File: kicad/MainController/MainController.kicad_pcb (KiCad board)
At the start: 2 copper layers, 45 parts, among them J1 Controller, J10 Barrel_Jack_Switch, J3 JTAG, J4 H-Bridge, J5 Lamp, J7 RGB, J8 Winch, J9 Motor, Q1 BC547, Q10 BUZ11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

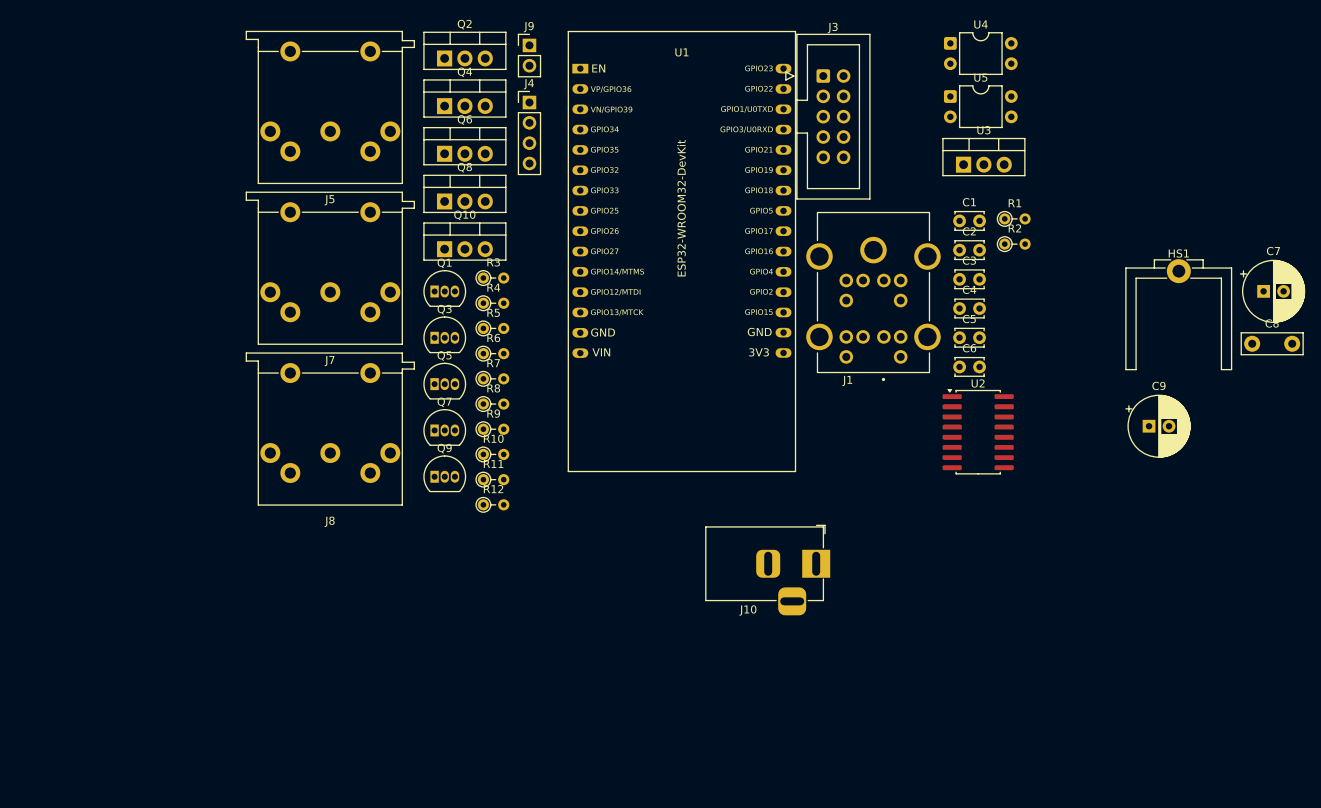
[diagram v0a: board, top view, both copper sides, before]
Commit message: New main controller PCB layout using ESP32
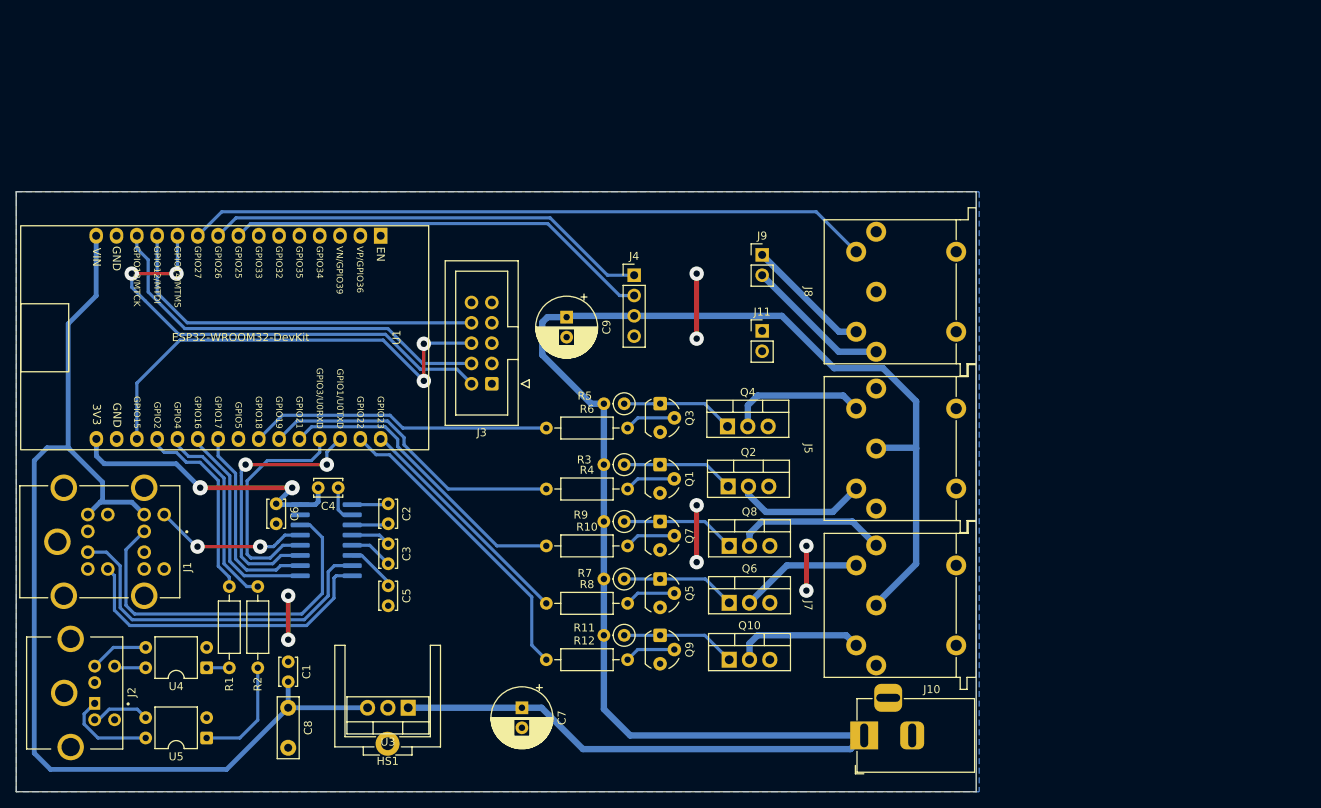
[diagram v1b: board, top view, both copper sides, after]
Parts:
- added J11: Pwr, Connector_PinHeader_2.54mm:PinHeader_1x02_P2.54mm_Vertical, F.Cu at (170.7, 85.4)
- added J2: Screen, SnapEDA:MiniDIN TE_5749180-1, F.Cu at (83.5, 130.7)
- Q1, Q3, Q5, Q7, Q9: footprint Package_TO_SOT_THT:TO-92_Inline -> Custom_Footprints:TO-92_Milling
- R1, R2: footprint Resistor_THT:R_Axial_DIN0204_L3.6mm_D1.6mm_P2.54mm_Vertical -> Resistor_THT:R_Axial_DIN0207_L6.3mm_D2.5mm_P10.16mm_Horizontal
- R10, R12, R4, R6, R8: value 220 -> 1k; footprint Resistor_THT:R_Axial_DIN0204_L3.6mm_D1.6mm_P2.54mm_Vertical -> Resistor_THT:R_Axial_DIN0207_L6.3mm_D2.5mm_P10.16mm_Horizontal
- R11, R3, R5, R7, R9: footprint Resistor_THT:R_Axial_DIN0204_L3.6mm_D1.6mm_P2.54mm_Vertical -> Resistor_THT:R_Axial_DIN0207_L6.3mm_D2.5mm_P2.54mm_Vertical
- U2: moved to B.Cu
- moved C8 128.8 mm to (111.5, 132.5), turned to -90 degrees
- moved U5 122.8 mm to (101.3, 136.3), turned to 180 degrees
- moved U4 121.4 mm to (101.3, 127.5), turned to 180 degrees
- moved J1 114.4 mm to (78.0, 111.8), turned to 90 degrees
- moved HS1 114.3 mm to (123.9, 136.1), turned to 180 degrees
- moved R1 107.3 mm to (104.1, 117.3), turned to -90 degrees
- moved C7 106.3 mm to (140.7, 132.5), turned to -90 degrees
- moved R2 102.7 mm to (107.7, 117.3), turned to -90 degrees
- moved C1 101.8 mm to (111.5, 129.2), turned to 90 degrees
- moved U3 97.1 mm to (126.5, 132.5), turned to 180 degrees
- moved C6 87.1 mm to (110.0, 107.0), turned to -90 degrees
- moved U2 82.6 mm to (116.2, 111.6), turned to 180 degrees
- moved C4 80.8 mm to (117.8, 105.0), turned to 180 degrees
- moved J5 78.9 mm to (185.0, 100.1), turned to -90 degrees
- moved C3 78.7 mm to (124.0, 112.0), turned to -90 degrees
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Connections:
- net Net-(J9-Pin_1) renamed /PowerConnectors/M1
- net Net-(J9-Pin_2) renamed /PowerConnectors/M2
- net Net-(Q10-D) renamed /PowerConnectors/LED_B
- net Net-(Q2-D) renamed /PowerConnectors/LED_L2
- net Net-(Q4-D) renamed /PowerConnectors/LED_L1
- net Net-(Q6-D) renamed /PowerConnectors/LED_G
- net Net-(Q8-D) renamed /PowerConnectors/LED_R
- J10 pad 3: unconnected-(J10-Pad3) -> GND
- J3 pad 1: /MOSI -> unconnected-(J3-Pin_1-Pad1)
- J3 pad 10: GND -> unconnected-(J3-Pin_10-Pad10)
- J3 pad 2: GND -> /TMS
- J3 pad 3: unconnected-(J3-Pin_3-Pad3) -> GND
- J3 pad 4: GND -> /TCK
- J3 pad 5: /Reset -> GND
- J3 pad 6: GND -> /TDO
- J3 pad 7: /SCK -> GND
- J3 pad 8: GND -> /TDI
- J3 pad 9: /MISO -> GND
- U1 pad 1: /Reset -> unconnected-(U1-EN-Pad1)
- U1 pad 10: /In2 -> /Switch
- U1 pad 11: unconnected-(U1-MTMS/GPIO14/ADC2_CH6-Pad11) -> /TMS
- U1 pad 12: unconnected-(U1-MTDI/GPIO12/ADC2_CH5-Pad12) -> /TDI
- U1 pad 13: unconnected-(U1-MTCK/GPIO13/ADC2_CH4-Pad13) -> /TCK
- U1 pad 18: unconnected-(U1-MTDO/GPIO15/ADC2_CH3-Pad18) -> /TDO
- U1 pad 19: /R -> /Screen_Up
- U1 pad 20: /G -> /Screen_Down
- U1 pad 23: /B -> unconnected-(U1-GPIO5-Pad23)
- U1 pad 26: /Screen_Down -> /R
- U1 pad 29: /Screen_Up -> /B
- U1 pad 30: /Switch -> /G
- U1 pad 8: unconnected-(U1-DAC_1/ADC2_CH8/GPIO25-Pad8) -> /In1
- U1 pad 9: /In1 -> /In2
- U2 pad 10: /SW_TXD -> /TXD
- U2 pad 11: /TXD -> /SW_TXD
- U2 pad 12: /RXD -> /SW_RXD
- U2 pad 13: /RS232_IN -> /SW_RS232_IN
- U2 pad 14: /RS232_OUT -> /SW_RS232_OUT
- U2 pad 7: /SW_RS232_OUT -> /RS232_OUT
- U2 pad 8: /SW_RS232_IN -> /RS232_IN
- U2 pad 9: /SW_RXD -> /RXD
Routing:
- net +12V: track 0.00 -> 230.1 mm
- net +5V: track 0.00 -> 135.4 mm
- net /Switch: track 0.00 -> 85.6 mm
- net /TMS: track 0.00 -> 59.5 mm, vias 0 -> 2
- net /TDO: track 0.00 -> 57.8 mm, vias 0 -> 2
- net /In2: track 0.00 -> 55.9 mm
- net /In1: track 0.00 -> 53.8 mm
- net /TCK: track 0.00 -> 51.7 mm
- net /TDI: track 0.00 -> 48.0 mm
- net /SW_RS232_OUT: track 0.00 -> 46.7 mm
- net /RS232_OUT: track 0.00 -> 44.2 mm
- net /RS232_IN: track 0.00 -> 40.1 mm
- net /Lamp2: track 0.00 -> 38.4 mm
- net +3.3V: track 0.00 -> 38.3 mm, vias 0 -> 2
- net /B: track 0.00 -> 38.2 mm
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- added copper zone on B.Cu, net GND
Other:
- board outline added: 120 x 75 mm

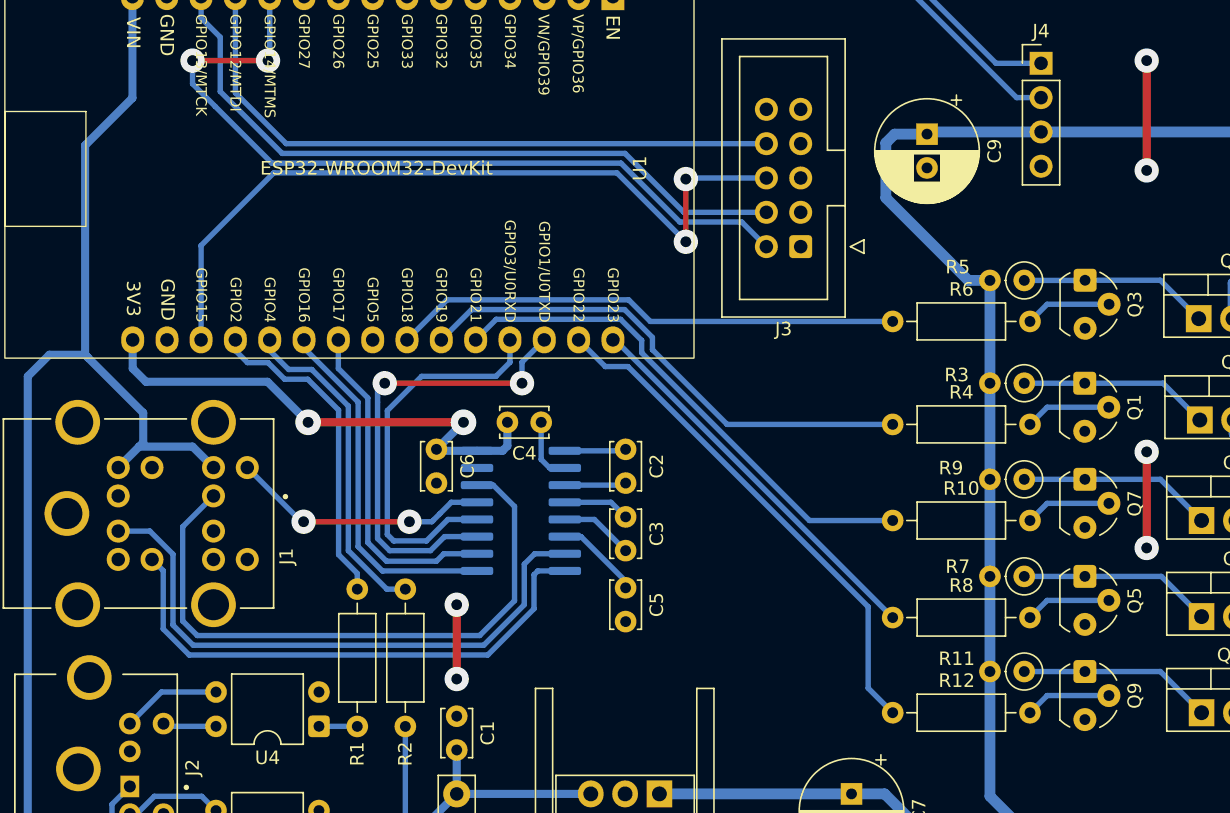
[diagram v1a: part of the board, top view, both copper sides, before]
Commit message: Updated main controller implementation for ESP32
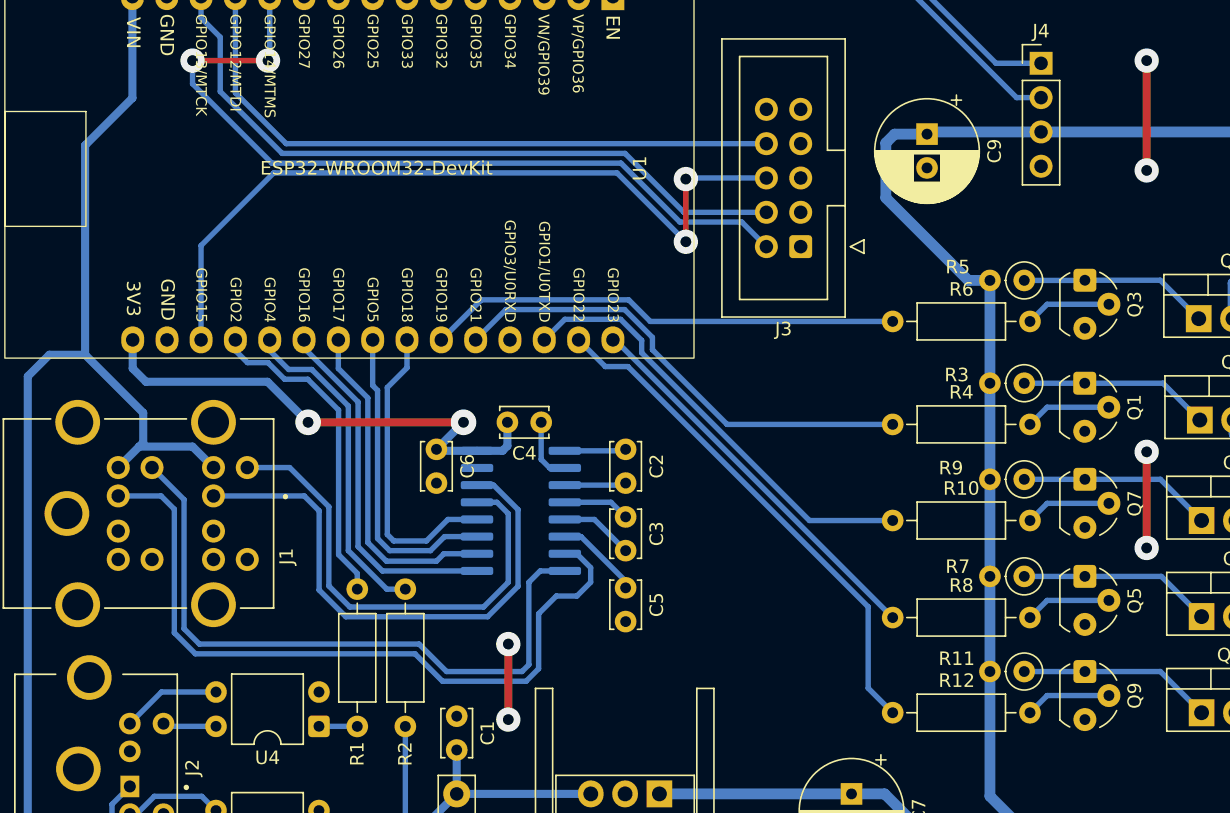
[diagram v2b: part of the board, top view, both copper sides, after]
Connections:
- net /RXD renamed /PR_RXD
- net /SW_RS232_IN renamed /KP_RS232_IN
- net /SW_RS232_OUT renamed /KP_RS232_OUT
- net /TXD renamed /PR_TXD
- J1 pad 1_1: /RS232_OUT -> unconnected-(J1-Pad1_1)
- J1 pad 2_1: unconnected-(J1-Pad2_1) -> /PR_RS232_OUT
- J1 pad 5_1: /RS232_IN -> unconnected-(J1-Pad5_1)
- J1 pad 6_1: unconnected-(J1-Pad6_1) -> /PR_RS232_IN
- U1 pad 23: unconnected-(U1-GPIO5-Pad23) -> /KP_TXD
- U1 pad 24: /Lamp1 -> /KP_RXD
- U1 pad 25: /Lamp2 -> /Lamp1
- U1 pad 26: /R -> /Lamp2
- U1 pad 27: /SW_RXD -> unconnected-(U1-U0RXD/GPIO3-Pad27)
- U1 pad 28: /SW_TXD -> /R
- U2 pad 11: /SW_TXD -> /KP_TXD
- U2 pad 12: /SW_RXD -> /KP_RXD
- U2 pad 7: /RS232_OUT -> /PR_RS232_OUT
- U2 pad 8: /RS232_IN -> /PR_RS232_IN
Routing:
- net /PR_RS232_OUT: track 0.00 -> 54.8 mm
- net /PR_RS232_IN: track 0.00 -> 49.1 mm
- net /RS232_OUT: track 44.2 -> 0.00 mm
- net /RS232_IN: track 40.1 -> 0.00 mm
- net /SW_TXD: track 33.9 -> 0.00 mm, vias 2 -> 0
- net /SW_RXD: track 28.9 -> 0.00 mm
- net /KP_TXD: track 0.00 -> 23.0 mm
- net /KP_RXD: track 0.00 -> 21.8 mm
- net /KP_RS232_IN: track 19.3 -> 35.5 mm, vias 2 -> 0
- net /KP_RS232_OUT: track 46.7 -> 40.1 mm
- net /R: track 38.2 -> 33.1 mm
- net /Lamp2: track 38.4 -> 35.8 mm
- net /Lamp1: track 37.8 -> 35.3 mm
- net Net-(Q3-C): track 14.8 -> 14.1 mm
- net /Screen_Up: track 24.6 -> 24.1 mm

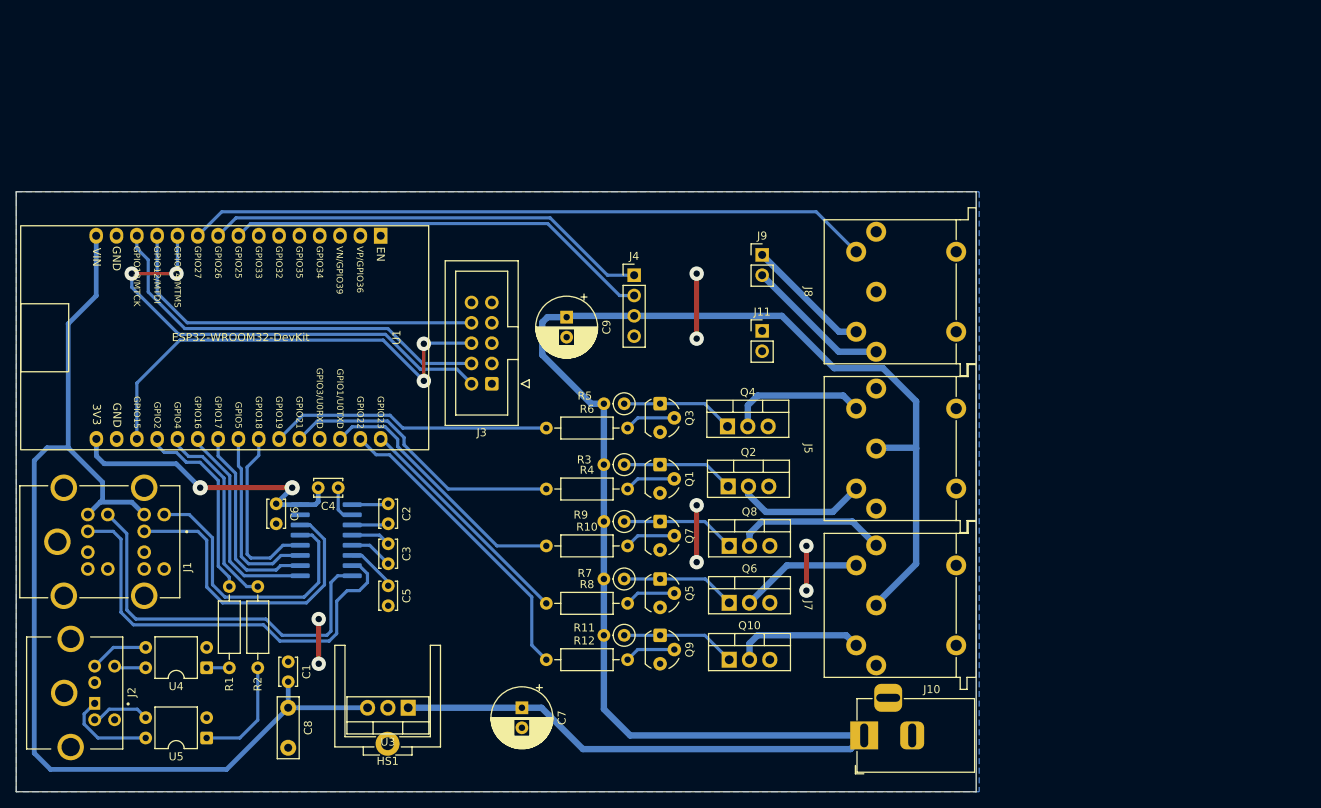
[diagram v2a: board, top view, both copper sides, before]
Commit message: Updated main controller for digital RGB strip
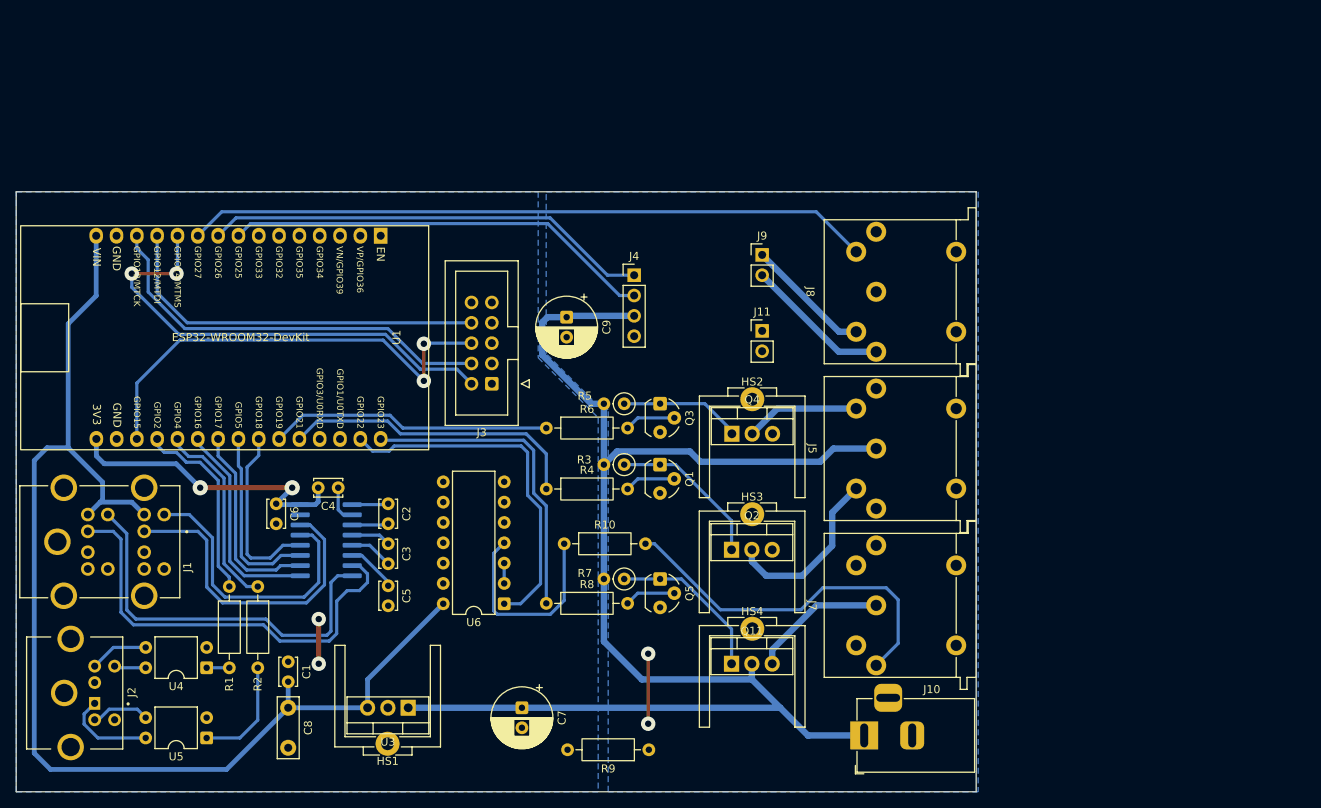
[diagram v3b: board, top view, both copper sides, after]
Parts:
- removed Q10, Q6, Q8: BUZ11, Package_TO_SOT_THT:TO-220-3_Vertical
- removed Q7, Q9: BC547, Custom_Footprints:TO-92_Milling
- removed R11: 10k, Resistor_THT:R_Axial_DIN0207_L6.3mm_D2.5mm_P2.54mm_Vertical
- removed R12: 1k, Resistor_THT:R_Axial_DIN0207_L6.3mm_D2.5mm_P10.16mm_Horizontal
- added HS2: Heatsink_Pad, Custom_Heatsinks:Heatsink_Aavid_TO-220_H12.7mm, F.Cu at (169.5, 94.8)
- added HS3: Heatsink_Pad, Custom_Heatsinks:Heatsink_Aavid_TO-220_H12.7mm, F.Cu at (169.5, 109.2)
- added HS4: Heatsink_Pad, Custom_Heatsinks:Heatsink_Aavid_TO-220_H12.7mm, F.Cu at (169.5, 123.5)
- added Q11: IRF4905, Package_TO_SOT_THT:TO-220-3_Vertical, F.Cu at (166.9, 127.0)
- added U6: 4069, Package_DIP:DIP-14_W7.62mm, F.Cu at (138.5, 119.5)
- R10: value 1k -> 100
- R9: value 10k -> 100; footprint Resistor_THT:R_Axial_DIN0207_L6.3mm_D2.5mm_P2.54mm_Vertical -> Resistor_THT:R_Axial_DIN0207_L6.3mm_D2.5mm_P10.16mm_Horizontal
- moved R9 28.7 mm to (156.6, 137.8)
- moved Q2 7.93 mm to (166.9, 112.8)
- moved R10 2.25 mm to (146.0, 112.0)
- moved Q4 1.07 mm to (167.0, 98.2)
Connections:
- net /G renamed /RGB_PWR
- C9 pad 2: GND -> GND2
- J10 pad 2: GND -> GND2
- J10 pad 3: GND -> GND2
- J4 pad 4: GND -> GND2
- J7 pad 1: /PowerConnectors/LED_R -> GND2
- J7 pad 2: +12V -> /PowerConnectors/LED_PWR
- J7 pad 3: unconnected-(J7-Pad3) -> Net-(J7-Pad3)
- J7 pad 4: /PowerConnectors/LED_G -> unconnected-(J7-Pad4)
- J7 pad 5: /PowerConnectors/LED_B -> unconnected-(J7-Pad5)
- J8 pad 1: GND -> GND2
- Q1 pad 3: GND -> GND2
- Q2 pad 3: GND -> GND2
- Q3 pad 3: GND -> GND2
- Q4 pad 3: GND -> GND2
- Q5 pad 3: GND -> GND2
- R10 pad 1: /R -> Net-(R10-Pad1)
- R10 pad 2: Net-(Q7-B) -> Net-(J7-Pad3)
- R9 pad 1: Net-(Q7-C) -> GND2
- R9 pad 2: +12V -> GND
- U1 pad 28: /R -> unconnected-(U1-U0TXD/GPIO1-Pad28)
- U1 pad 29: /B -> /RGB_Data
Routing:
- net +12V: track 230.1 -> 177.4 mm
- net Net-(J7-Pad3): track 0.00 -> 46.1 mm
- net /RGB_Data: track 0.00 -> 44.8 mm
- net /B: track 38.2 -> 0.00 mm
- net /R: track 33.1 -> 0.00 mm
- net Net-(R10-Pad1): track 0.00 -> 25.9 mm
- net GND: track 26.4 -> 5.59 mm, vias 8 -> 2
- net /PowerConnectors/LED_R: track 19.2 -> 0.00 mm
- net /PowerConnectors/LED_PWR: track 0.00 -> 17.0 mm
- net +5V: track 135.4 -> 152.3 mm
- net /PowerConnectors/LED_B: track 16.3 -> 0.00 mm
- net /PowerConnectors/LED_G: track 15.3 -> 0.00 mm
- net Net-(Q7-C): track 14.4 -> 0.00 mm
- net Net-(Q10-G): track 14.4 -> 0.00 mm
- net /RGB_PWR: track 29.2 -> 39.3 mm
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- added copper zone on B.Cu, net GND2
